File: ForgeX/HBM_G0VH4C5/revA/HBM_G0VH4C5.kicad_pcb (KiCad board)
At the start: 2 copper layers, 32.2 x 69.6 mm, 34 parts, among them J1 Conn_02x05_Odd_Even, J2 Screw_Terminal_01x03, Q1 STF24N60M2, Q2 STF24N60M2, U1 INA199xxDCK, U3 L6388ED, U7 AMS1117-3.3

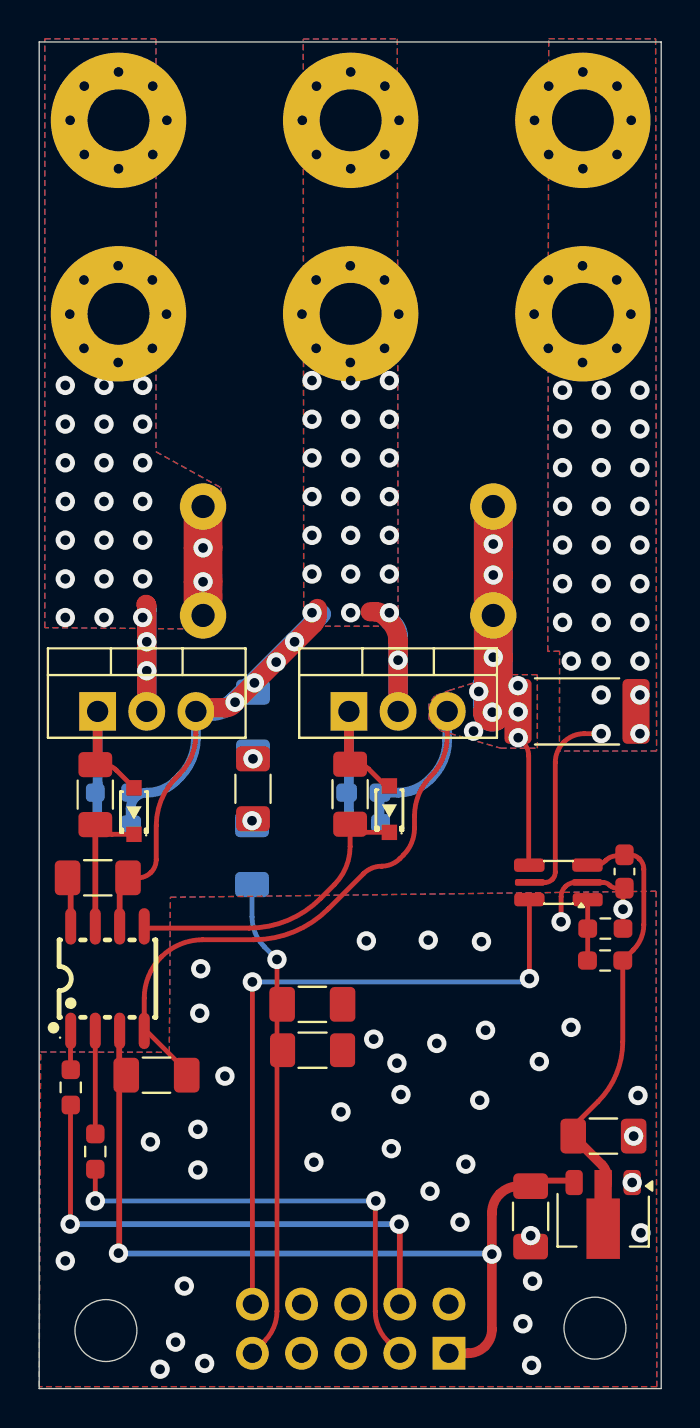
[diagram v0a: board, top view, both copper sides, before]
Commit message: BlackDev Fini & HBM mod
Finalized blackDev, HBM with (RC) ground coupling, LVP swapping RS422 to RS485 and processing card interface modifications
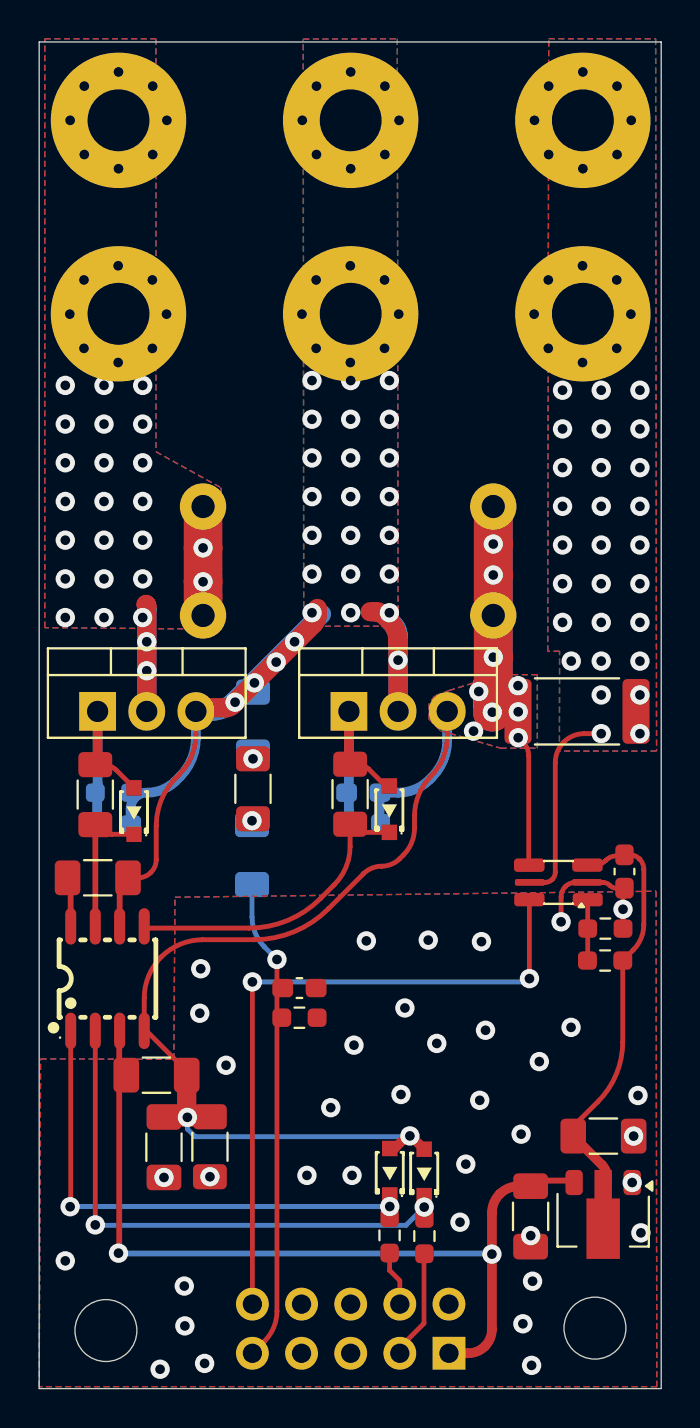
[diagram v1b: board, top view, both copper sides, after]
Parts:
- added C10: 100p, Capacitor_SMD:C_1206_3216Metric_Pad1.33x1.80mm_HandSolder, F.Cu at (170.2, 101.6)
- added D3: SD103AWS_C5345966, EasyEDA:SOD-323_L1.7-W1.3-LS2.5-RD, F.Cu at (183.6, 102.9)
- added D4: SD103AWS_C5345966, EasyEDA:SOD-323_L1.7-W1.3-LS2.5-RD, F.Cu at (181.8, 102.9)
- added R8: 220, Resistor_SMD:R_1206_3216Metric_Pad1.30x1.75mm_HandSolder, F.Cu at (172.5, 101.6)
- C9: footprint Capacitor_SMD:C_1206_3216Metric_Pad1.33x1.80mm_HandSolder -> Capacitor_SMD:C_0603_1608Metric_Pad1.08x0.95mm_HandSolder
- R26: footprint Resistor_SMD:R_1206_3216Metric_Pad1.30x1.75mm_HandSolder -> Resistor_SMD:R_0603_1608Metric_Pad0.98x0.95mm_HandSolder
- moved R6 18.2 mm to (181.8, 106.2)
- moved R7 17.6 mm to (183.6, 106.2)
- moved R26 1.81 mm to (177.2, 94.9)
- moved C9 1.07 mm to (177.2, 93.4)
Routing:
- net Net-(D4-K): track 2.01 -> 26.8 mm, vias 0 -> 2
- net LIN: track 27.3 -> 2.86 mm, vias 2 -> 0
- net Net-(D3-K): track 5.33 -> 28.6 mm, vias 0 -> 2
- net HIN: track 24.4 -> 5.75 mm, vias 2 -> 0
- net /Shunt+: track 66.5 -> 84.9 mm, vias 9 -> 11
- net GND: vias 38 -> 37

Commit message: G0 images added for doc
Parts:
- added G***: LOGO, LOGO, F.Cu at (180.0, 64.6)
